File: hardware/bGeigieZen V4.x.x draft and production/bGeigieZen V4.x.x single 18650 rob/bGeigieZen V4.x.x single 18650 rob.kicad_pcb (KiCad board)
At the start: 2 copper layers, 129.4 x 64.6 mm, 14 parts, among them J1 M5 2x15 pin, J2 Geiger IRover, J3 GPS, J4 Geiger Safepulse, J5 Extra support header

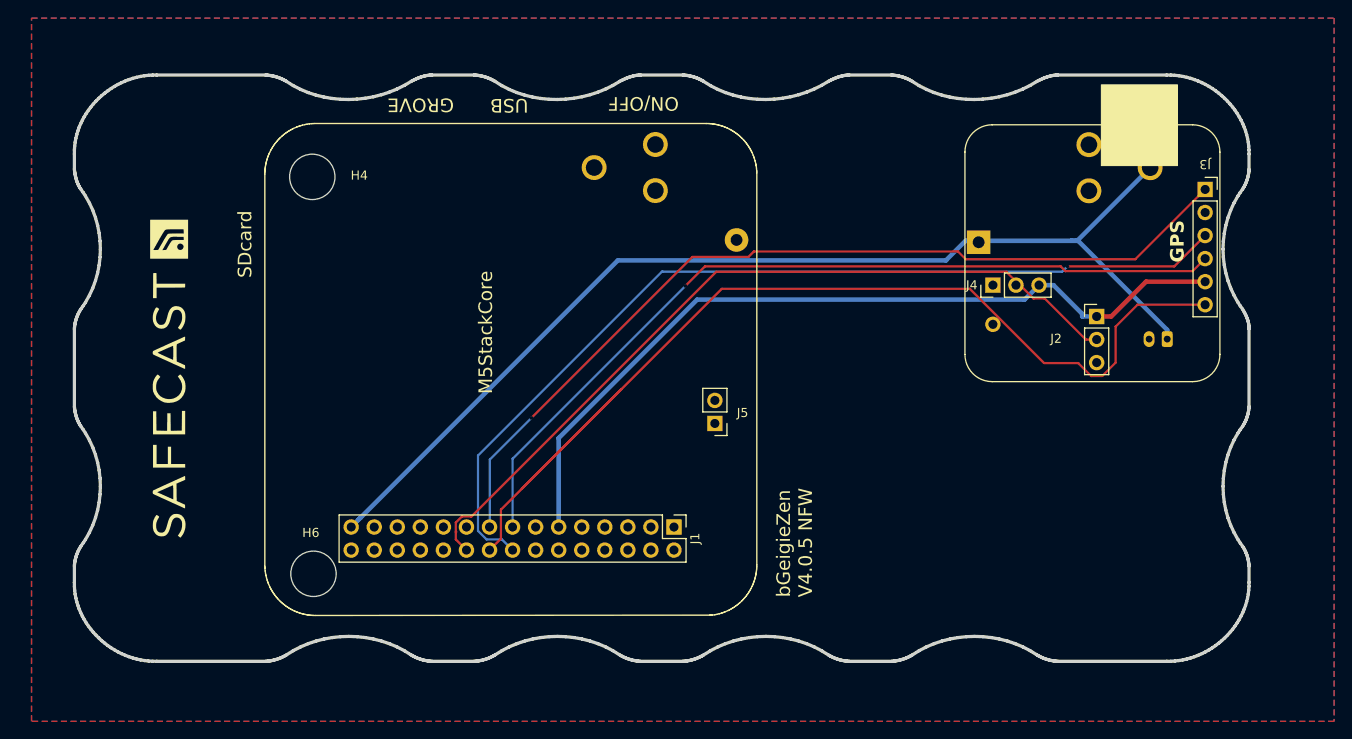
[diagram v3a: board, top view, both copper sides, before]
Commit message: added fuse to the 4.0.5 NFW board. Just to be safe:)
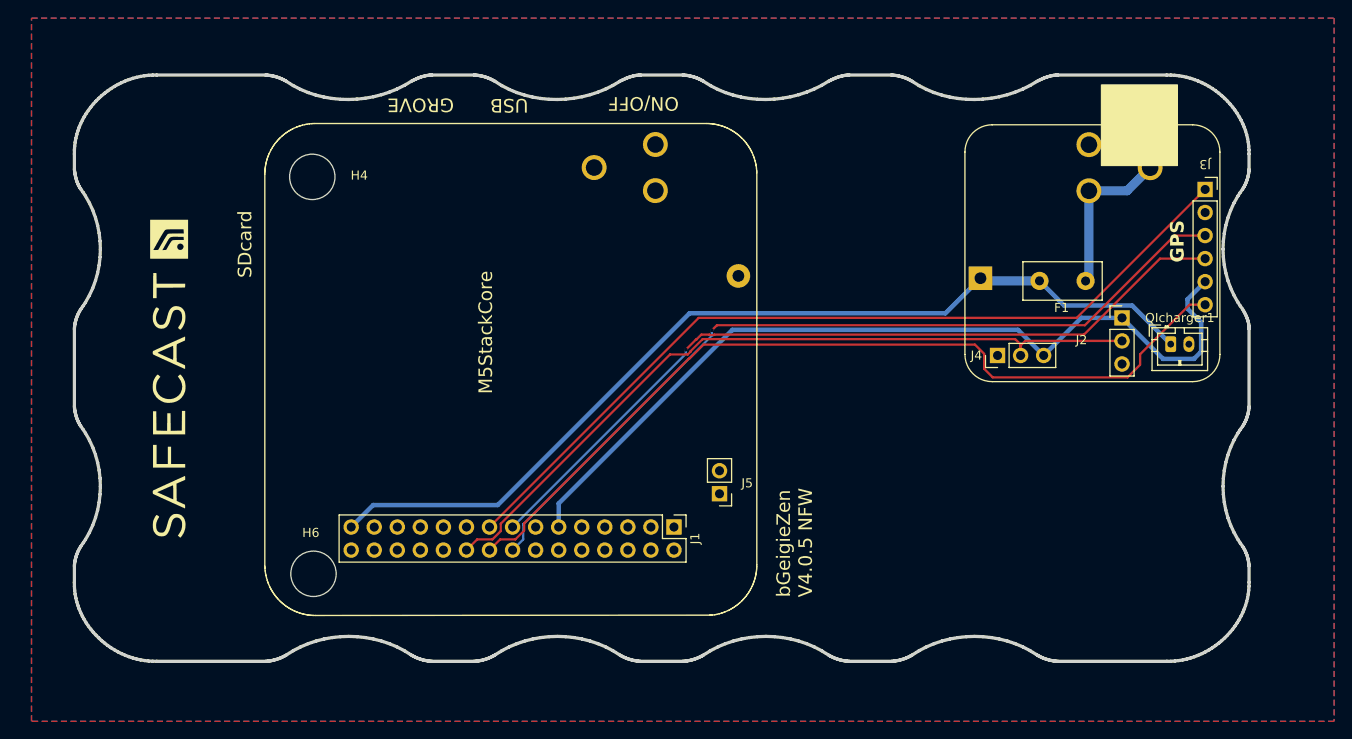
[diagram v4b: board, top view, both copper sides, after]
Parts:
- removed ?: , 
- removed Crowbar: Crowbar, Diode_THT:D_DO-201_P15.24mm_Horizontal
- removed QI: QI GND, Connector_JST:JST_PH_B2B-PH-K_1x02_P2.00mm_Vertical
- added D1: Crowbar, Diode_THT:D_DO-201_P15.24mm_Horizontal, B.Cu at (178.1, 89.1)
- added F1: Fuse_Small, Fuse:Fuse_Littelfuse_395Series, F.Cu at (196.0, 89.4)
- added QIcharger1: QI GND, Connector_JST:JST_PH_B2B-PH-K_1x02_P2.00mm_Vertical, F.Cu at (205.4, 96.3)
- BT1: value 3.7 V Lipo -> 3.7 V Lipo
- moved J4 7.76 mm to (186.3, 97.6)
- moved J5 7.76 mm to (155.7, 112.8)
- moved J2 2.80 mm to (200.0, 93.4)
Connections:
- BT1 pad 1: /BAT -> Net-(BT1-+)
- BT1 pad PWR@2: (no net) -> Net-(BT1-+)
- BT1 pad PWR@3: (no net) -> Net-(BT1-+)
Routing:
- net Net-(BT1-+): track 0.00 -> 26.3 mm
- net /SCL: track 117.7 -> 95.1 mm
- net /BAT: track 120.9 -> 104.7 mm
- net /TX2: track 103.2 -> 92.0 mm
- net /SDA: track 99.3 -> 94.2 mm, vias 1 -> 0
- net /RX2: track 93.4 -> 88.9 mm
- net 3.3V: track 91.2 -> 95.5 mm
- net /GIO2 on Core and GIO32 on Core-2: track 89.3 -> 85.1 mm

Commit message: Updated 4.x.x boards and 3.0.3a  with isolated positive battery for filling planes.
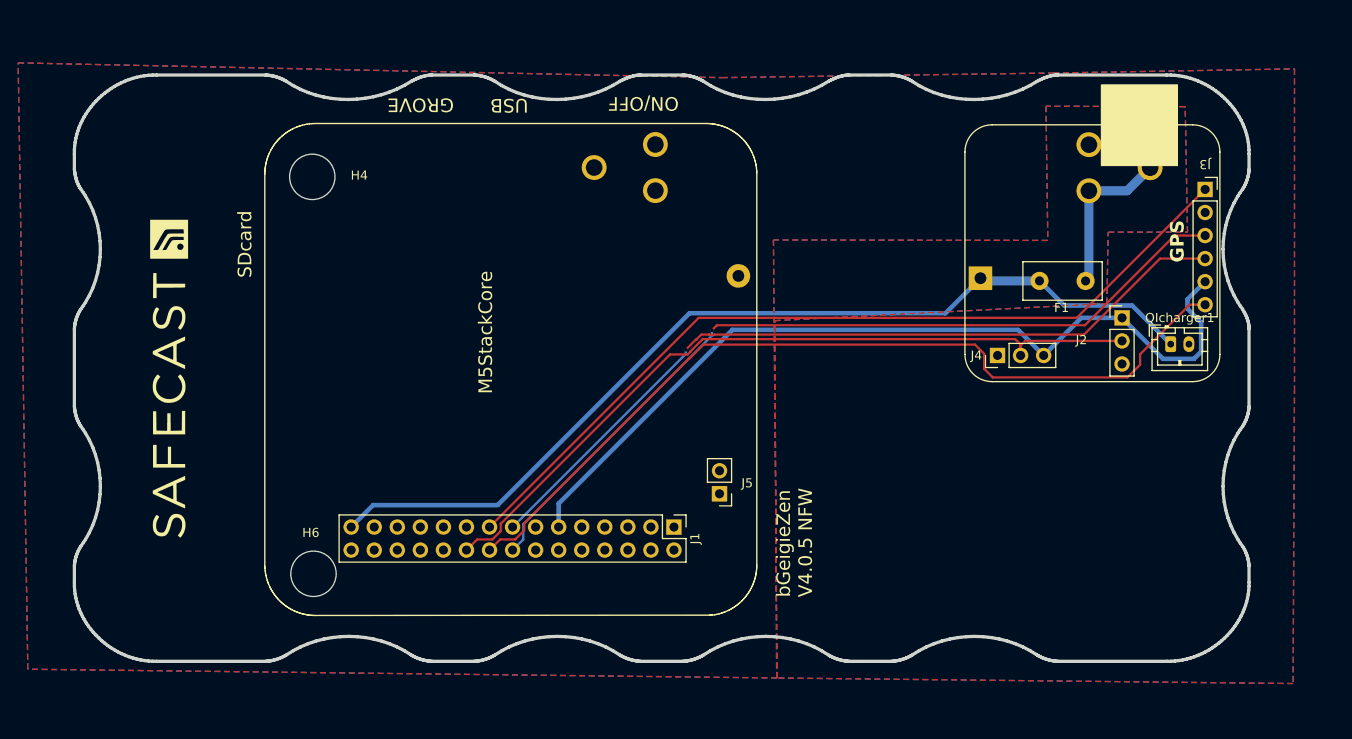
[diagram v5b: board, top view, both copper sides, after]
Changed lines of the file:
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@@
 		(tags "Fuse TE5 Littelfuse/Wickmann No. 460 No560 ")
 		(property "Reference" "F1"
-			(at 2.65 -2.95 360)
+			(at 2.65 -2.95 0)
 			(layer "F.SilkS")
 			(effects
@@
 		)
 		(property "Value" "Fuse_Small"
-			(at 2.35 3.1 360)
+			(at 2.35 3.1 0)
 			(layer "F.Fab")
 			(effects
@@
 		)
 		(fp_text user "${REFERENCE}"
-			(at 2.75 -1.25 360)
+			(at 2.75 -1.25 0)
 			(layer "F.Fab")
 			(effects
@@
 		)
 		(property "Sim.Device" "D"
-			(at 0 0 0)
-			(unlocked yes)
-			(layer "B.Fab")
-			(hide yes)
-			(effects
-				(font
-					(size 1 1)
-					(thickness 0.15)
-				)
-				(justify mirror)
-			)
-		)
-		(property "Sim.Pins" "1=K 2=A"
-			(at 0 0 0)
-			(unlocked yes)
-			(layer "B.Fab")
-			(hide yes)
-			(effects
-				(font
-					(size 1 1)
-					(thickness 0.15)
-				)
-				(justify mirror)
-			)
-		)
-		(property "Sim.Device" "D"
 			(at 0.762 0.066 0)
 			(unlocked yes)
@@
 		(min_thickness 0.254)
 		(filled_areas_thickness no)
-		(fill yes
+		(fill
 			(thermal_gap 0.508)
 			(thermal_bridge_width 0.508)
@@
 		(polygon
 			(pts
-				(xy 223.3676 60.4) (xy 223.3676 137.87) (xy 79.8576 137.87) (xy 79.8576 60.4)
+				(xy 155.9052 66.9532) (xy 192.4304 66.4452) (xy 218.9988 65.988) (xy 218.9988 101.1416) (xy 218.8464 133.7044)
+				(xy 161.9504 133.0948) (xy 161.7472 93.7248) (xy 198.3232 91.8452) (xy 198.4756 83.9712) (xy 207.2132 83.9712)
+				(xy 206.9592 70.1536) (xy 191.6176 70.1028) (xy 191.8208 84.8856) (xy 161.5948 84.8348) (xy 162.0012 133.0948)
+				(xy 79.4512 132.1296) (xy 78.3844 65.3276)
 			)
 		)

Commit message: Mini  fuse added and 3d files for 4.0.5 NFW
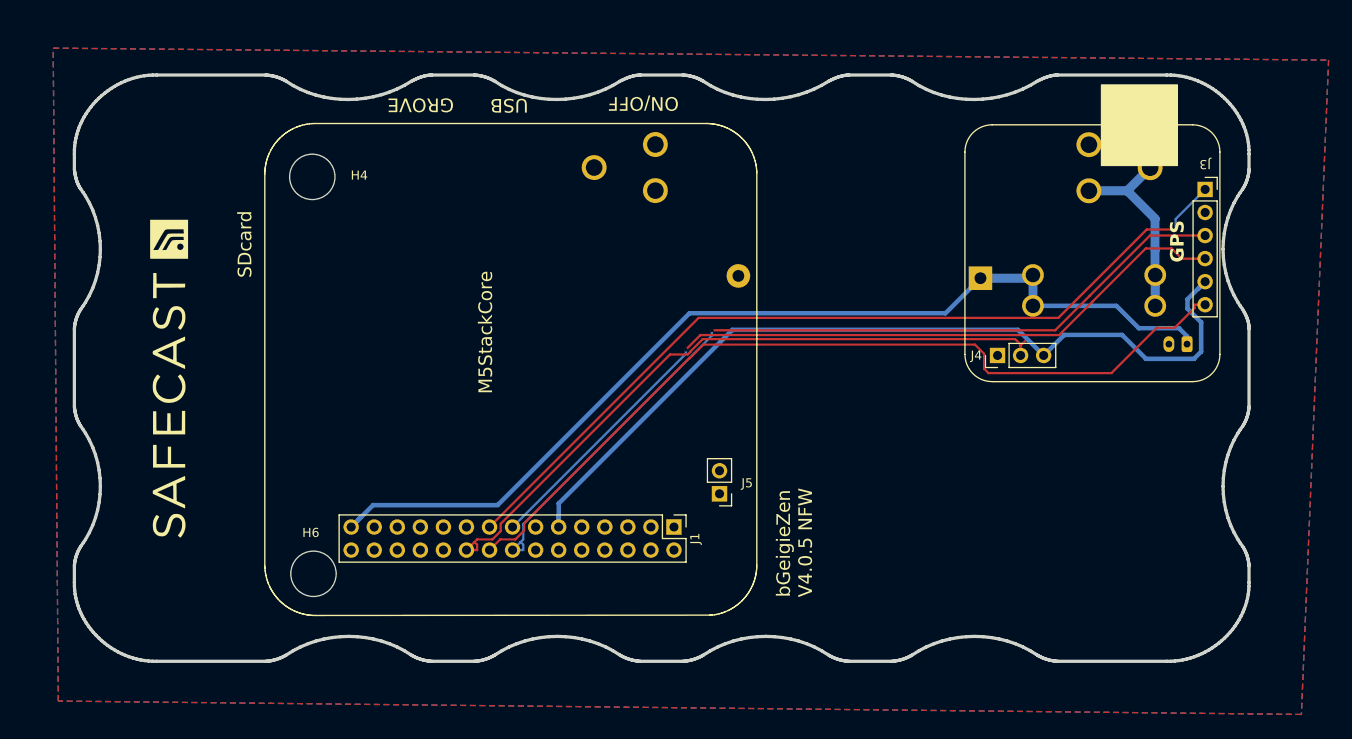
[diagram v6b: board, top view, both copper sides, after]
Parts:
- removed J2: Geiger IRover, Connector_PinHeader_2.54mm:PinHeader_1x03_P2.54mm_Vertical
- F1: footprint Fuse:Fuse_Littelfuse_395Series -> bGeigieZen:FUSE_3557-2; moved to B.Cu
- QIcharger1: moved to B.Cu
- moved QIcharger1 1.80 mm to (207.2, 96.3), turned to 180 degrees
- moved F1 1.40 mm to (196.9, 90.4)
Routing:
- net /GIO2 on Core and GIO32 on Core-2: track 85.1 -> 74.7 mm
- net Net-(BT1-+): track 26.3 -> 32.9 mm
- net /BAT: track 104.7 -> 110.4 mm
- net /TX2: track 92.0 -> 93.3 mm
- net /RX2: track 88.9 -> 90.2 mm
- net /SDA: track 94.2 -> 95.1 mm, vias 0 -> 1
- net 3.3V: track 95.5 -> 96.3 mm
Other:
- board text removed: "Irover"

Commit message: Updated 3.0.6 board
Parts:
- Fuse 2A: renamed from F1
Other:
- board text added: "bGeigieZen V4.0.6 NFW"
- board text removed: "bGeigieZen V4.0.5 NFW"
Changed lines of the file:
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@@
 	(paper "A4")
 	(title_block
-		(title "bGeigieZen Draft V4.0.5 NFW")
+		(title "bGeigieZen Draft V4.0.6 NFW")
 		(date "2024-06-17")
-		(rev "V4.0.5 rob")
+		(rev "V4.0.6 rob")
 		(comment 1 "Not For Whimps version.")
 	)
@@
 			)
 			(scale
-				(xyz 1.8 1.8 1.8)
+				(xyz 1.8 1.1 1.1)
 			)
 			(rotate
@@
 		(tags "connector JST PH side entry")
 		(property "Reference" "QIcharger1"
-			(at 1 2.9 360)
+			(at 1 2.9 0)
 			(layer "B.SilkS")
 			(effects
@@
 		)
 		(property "Value" "QI GND"
-			(at 1 -4 360)
+			(at 1 -4 0)
 			(layer "B.Fab")
 			(effects
@@
 		)
 		(fp_text user "${REFERENCE}"
-			(at 1 -1.5 360)
+			(at 1 -1.5 0)
 			(layer "B.Fab")
 			(effects
@@
 		(layer "B.Cu")
 		(at 196.9222 90.3992 180)
-		(property "Reference" "F1"
-			(at -6.985 4.445 0)
+		(property "Reference" "Fuse 2A"
+			(at 0.0722 -4.24 0)
 			(layer "B.SilkS")
 			(effects
@@
 		(layer "Edge.Cuts")
 	)
-	(gr_text "bGeigieZen\nV4.0.5 NFW"
+	(gr_text "bGeigieZen\nV4.0.6 NFW"
 		(at 200.5584 112.724 90)
 		(layer "B.SilkS")
@@
 		)
 	)
-	(gr_text "bGeigieZen\nV4.0.5 NFW\n"
+	(gr_text "bGeigieZen\nV4.0.6 NFW\n"
 		(at 163.9316 124.2048 90)
 		(layer "F.SilkS")
@@
 		(polygon
 			(pts
-				(xy 193.1416 70.4076) (xy 207.518 70.6616) (xy 206.9592 92.8612) (xy 187.5536 92.8612) (xy 187.5536 83.3616)
+				(xy 193.1416 70.4076) (xy 207.518 70.6616) (xy 207.0608 94.182) (xy 187.6552 94.182) (xy 187.5536 83.3616)
 				(xy 193.1416 83.26)
 			)

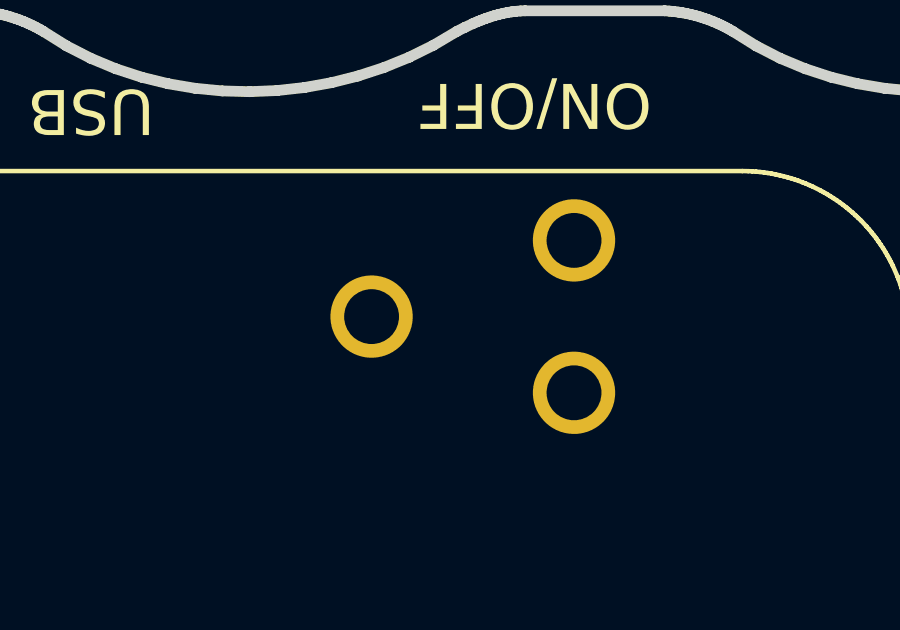
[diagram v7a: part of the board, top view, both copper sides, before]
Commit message: Update V3.x.x and V4.x.x board with updated 18650 footprints.
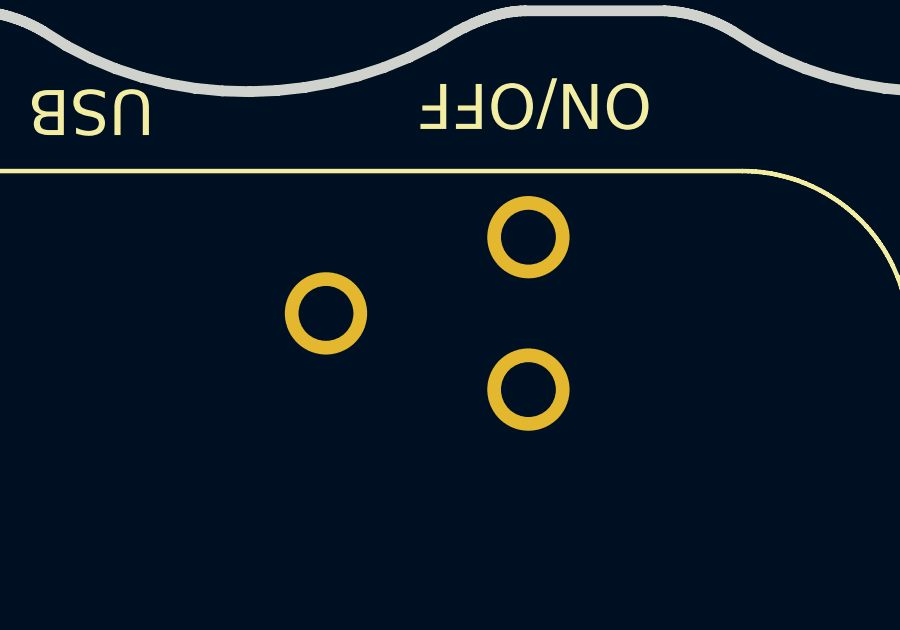
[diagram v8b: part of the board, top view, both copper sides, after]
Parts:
- moved G*** 1.32 mm to (165.7, 76.8)
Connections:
- BT1 pad 1: Net-(BT1-+) -> GND
- BT1 pad PWR@2: Net-(BT1-+) -> GND
- BT1 pad PWR@3: Net-(BT1-+) -> GND
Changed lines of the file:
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@@
 (kicad_pcb
-	(version 20240609)
+	(version 20240617)
 	(generator "pcbnew")
 	(generator_version "8.99")
@@
 	(title_block
 		(title "bGeigieZen Draft V4.0.6 NFW")
-		(date "2024-06-17")
+		(date "2024-06-20")
 		(rev "V4.0.6 rob")
 		(comment 1 "Not For Whimps version.")
@@
 	(footprint "bGeigieRaku_M5_1015:18650 map"
 		(layer "B.Cu")
-		(at 164.3785 76.8692 -90)
+		(at 165.6953 76.7576 -90)
 		(property "Reference" "G***"
 			(at 0 0 90)
@@
 		(attr through_hole)
 		(fp_rect
-			(start 5.1435 -22.86)
-			(end -5.1435 8.255)
+			(start 5.1435 -24.13)
+			(end -5.1435 14.097)
 			(stroke
 				(width 0.5)
@@
 		)
 		(fp_rect
-			(start 2.2225 -24.638)
-			(end -2.2225 -22.733)
+			(start 2.2225 -25.908)
+			(end -2.2225 -24.003)
 			(stroke
 				(width 0.1)
@@
 		)
 		(fp_text user "Protected 18650"
-			(at 1.016 -14.224 0)
+			(at 1.016 -12.192 0)
 			(unlocked yes)
 			(layer "B.SilkS")
@@
 		)
 		(fp_text user "-"
-			(at -2.032 5.08 90)
+			(at -2.286 9.144 90)
 			(unlocked yes)
 			(layer "B.SilkS")
@@
 			(at -27.6352 0 90)
 			(layer "B.SilkS")
+			(hide yes)
 			(effects
 				(font
@@
 		(attr through_hole)
 		(fp_line
-			(start 34.2448 4.455)
-			(end 30.765 4.455)
+			(start 35.56 4.572)
+			(end 28.733 4.572)
 			(stroke
 				(width 0.2032)
@@
 		)
 		(fp_line
-			(start 34.2448 -4.435)
-			(end 34.2448 4.455)
+			(start 35.56 -4.318)
+			(end 35.56 4.572)
 			(stroke
 				(width 0.2032)
@@
 		)
 		(fp_line
-			(start 30.765 5.5726)
-			(end 21.23 5.5726)
+			(start 28.733 5.6896)
+			(end 23.114 5.6896)
 			(stroke
 				(width 0.2032)
@@
 		)
 		(fp_line
-			(start 30.765 4.455)
-			(end 30.765 5.5726)
+			(start 28.733 4.572)
+			(end 28.733 5.6896)
 			(stroke
 				(width 0.2032)
@@
 		)
 		(fp_line
-			(start 30.765 -4.435)
-			(end 34.2448 -4.435)
+			(start 28.733 -4.318)
+			(end 35.56 -4.318)
 			(stroke
 				(width 0.2032)
@@
 		)
 		(fp_line
-			(start 30.765 -5.5526)
-			(end 30.765 -4.435)
+			(start 28.733 -5.4356)
+			(end 28.733 -4.318)
 			(stroke
 				(width 0.2032)
@@
 		)
 		(fp_line
-			(start 21.23 5.5726)
-			(end 21.23 -5.5526)
+			(start 23.114 5.6896)
+			(end 23.114 -5.4356)
 			(stroke
 				(width 0.2032)
@@
 		)
 		(fp_line
-			(start 21.23 -5.5526)
-			(end 30.765 -5.5526)
+			(start 23.114 -5.4356)
+			(end 28.733 -5.4356)
 			(stroke
 				(width 0.2032)
@@
 		)
 		(fp_line
-			(start 34.3248 4.445)
-			(end 30.845 4.445)
+			(start 35.56 4.572)
+			(end 28.813 4.562)
 			(stroke
 				(width 0.2032)
@@
 		)
 		(fp_line
-			(start 34.3248 -4.445)
-			(end 34.3248 4.445)
+			(start 35.56 -4.318)
+			(end 35.56 4.572)
 			(stroke
 				(width 0.2032)
@@
 		)
 		(fp_line
-			(start 34.2448 4.455)
-			(end 30.765 4.455)
+			(start 35.56 -4.318)
+			(end 35.56 4.572)
 			(stroke
 				(width 0.2032)
@@
 		)
 		(fp_line
-			(start 34.2448 -4.435)
-			(end 34.2448 4.455)
+			(start 32.2128 4.572)
+			(end 28.733 4.572)
 			(stroke
 				(width 0.2032)
@@
 		)
 		(fp_line
-			(start 30.845 5.5626)
-			(end 21.32 5.5626)
+			(start 28.813 5.6796)
+			(end 23.114 5.6896)
 			(stroke
 				(width 0.2032)
@@
 		)
 		(fp_line
-			(start 30.845 4.445)
-			(end 30.845 5.5626)
+			(start 28.813 4.562)
+			(end 28.813 5.6796)
 			(stroke
 				(width 0.2032)
@@
 		)
 		(fp_line
-			(start 30.845 -4.445)
-			(end 34.3248 -4.445)
+			(start 28.813 -4.328)
+			(end 35.56 -4.318)
 			(stroke
 				(width 0.2032)
@@
 		)
 		(fp_line
-			(start 30.845 -5.5626)
-			(end 30.845 -4.445)
+			(start 28.813 -5.4456)
+			(end 28.813 -4.328)
 			(stroke
 				(width 0.2032)
@@
 		)
 		(fp_line
-			(start 30.765 5.5726)
-			(end 21.23 5.5726)
+			(start 28.733 5.6896)
+			(end 23.114 5.6896)
 			(stroke
 				(width 0.2032)
@@
 		)
 		(fp_line
-			(start 30.765 4.455)
-			(end 30.765 5.5726)
+			(start 28.733 4.572)
+			(end 28.733 5.6896)
 			(stroke
 				(width 0.2032)
@@
 		)
 		(fp_line
-			(start 30.765 -4.435)
-			(end 34.2448 -4.435)
+			(start 28.733 -4.318)
+			(end 32.2128 -4.318)
 			(stroke
 				(width 0.2032)
@@
 		)
 		(fp_line
-			(start 30.765 -5.5526)
-			(end 30.765 -4.435)
+			(start 28.733 -5.4356)
+			(end 28.733 -4.318)
 			(stroke
 				(width 0.2032)
@@
 		)
 		(fp_line
-			(start 21.32 5.5626)
-			(end 21.32 -5.5626)
+			(start 23.114 5.6896)
+			(end 23.114 -5.4356)
 			(stroke
 				(width 0.2032)
@@
 		)
 		(fp_line
-			(start 21.32 -5.5626)
-			(end 30.845 -5.5626)
+			(start 23.114 5.6896)
+			(end 23.114 -5.4356)
 			(stroke
 				(width 0.2032)
@@
 		)
 		(fp_line
-			(start 21.23 5.5726)
-			(end 21.23 -5.5526)
+			(start 23.114 -5.4356)
+			(end 28.813 -5.4456)
 			(stroke
 				(width 0.2032)
@@
 		)
 		(fp_line
-			(start 21.23 -5.5526)
-			(end 30.765 -5.5526)
+			(start 23.114 -5.4356)
+			(end 28.733 -5.4356)
 			(stroke
 				(width 0.2032)
@@
 			(pintype "input")
 		)
-		(pad "2" thru_hole circle
-			(at 30.628 0.01)
+		(pad "1" thru_hole circle
+			(at 32.148 0.117)
 			(size 2.7432 2.7432)
 			(drill 1.8288)
@@
 			(remove_unused_layers no)
 			(net 1 "GND")
-			(pinfunction "-")
+			(pinfunction "+")
 			(pintype "input")
 		)
-		(pad "GND@2" thru_hole circle
-			(at 23.88 2.55 270)
+		(pad "PWR@2" thru_hole circle
+			(at -23.88 2.53 90)
 			(size 2.7432 2.7432)
 			(drill 1.8288)
@@
 			(remove_unused_layers no)
 		)
-		(pad "GND@3" thru_hole circle
-			(at 23.88 -2.53 270)
+		(pad "PWR@2" thru_hole circle
+			(at 25.4 -2.423 270)
 			(size 2.7432 2.7432)
 			(drill 1.8288)
 			(layers "*.Cu" "*.Mask")
 			(remove_unused_layers no)
+			(net 1 "GND")
 		)
-		(pad "PWR@2" thru_hole circle
-			(at -23.88 2.53 90)
+		(pad "PWR@3" thru_hole circle
+			(at -23.88 -2.55 90)
 			(size 2.7432 2.7432)
 			(drill 1.8288)
 			(layers "*.Cu" "*.Mask")
 			(remove_unused_layers no)
-			(net 31 "Net-(BT1-+)")
 		)
 		(pad "PWR@3" thru_hole circle
-			(at -23.88 -2.55 90)
+			(at 25.4 2.657 270)
 			(size 2.7432 2.7432)
 			(drill 1.8288)
 			(layers "*.Cu" "*.Mask")
 			(remove_unused_layers no)
-			(net 31 "Net-(BT1-+)")
+			(net 1 "GND")
 		)
 		(model "${KIPRJMOD}/shapes3D/KEYELCO_54.wrl"
